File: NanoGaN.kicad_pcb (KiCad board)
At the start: 6 copper layers, 54 x 94 mm, 221 parts, among them J1 U_DC, J10 Conn_01x06, J11 Conn_01x04, J12 USB4085-GF-A, J14 Conn_01x03, J2 GND, J3 Phase_U, J4 Phase_V, J5 Phase_W, J6 FTSH-107-01-L-DV-K-TR, J7 Conn_01x03, J8 Conn_01x02, J9 Conn_01x07, Q1 IGC025S08S1, Q2 IGC025S08S1, Q3 IGC025S08S1, Q4 IGC025S08S1, Q5 IGC025S08S1, Q6 IGC025S08S1, Q7 Si2302CDS, U1 STM32H723VGTx, U10 SN74LVC1G66DCKR, U11 SN74LVC1G66DCKR, U12 LMG1205YFXR, U13 BMI323, U14 AS5047P-ATST, U15 TCAN1044VDRQ1, U16 SN74LVC1G66DCKR, U17 AD8418, U18 SN74LVC1G66DCKR, U19 NCS2220AMUT1G, U2 LMR51635XDDCR, U20 NCS2220AMUT1G, U21 NCS2220AMUT1G, U3 AMS1117, U4 AD8418, U5 LMG1205YFXR, U6 SN74LVC1G66DCKR, U7 SN74LVC1G66DCKR, U8 LMG1205YFXR, U9 AD8418, X1 8MHz

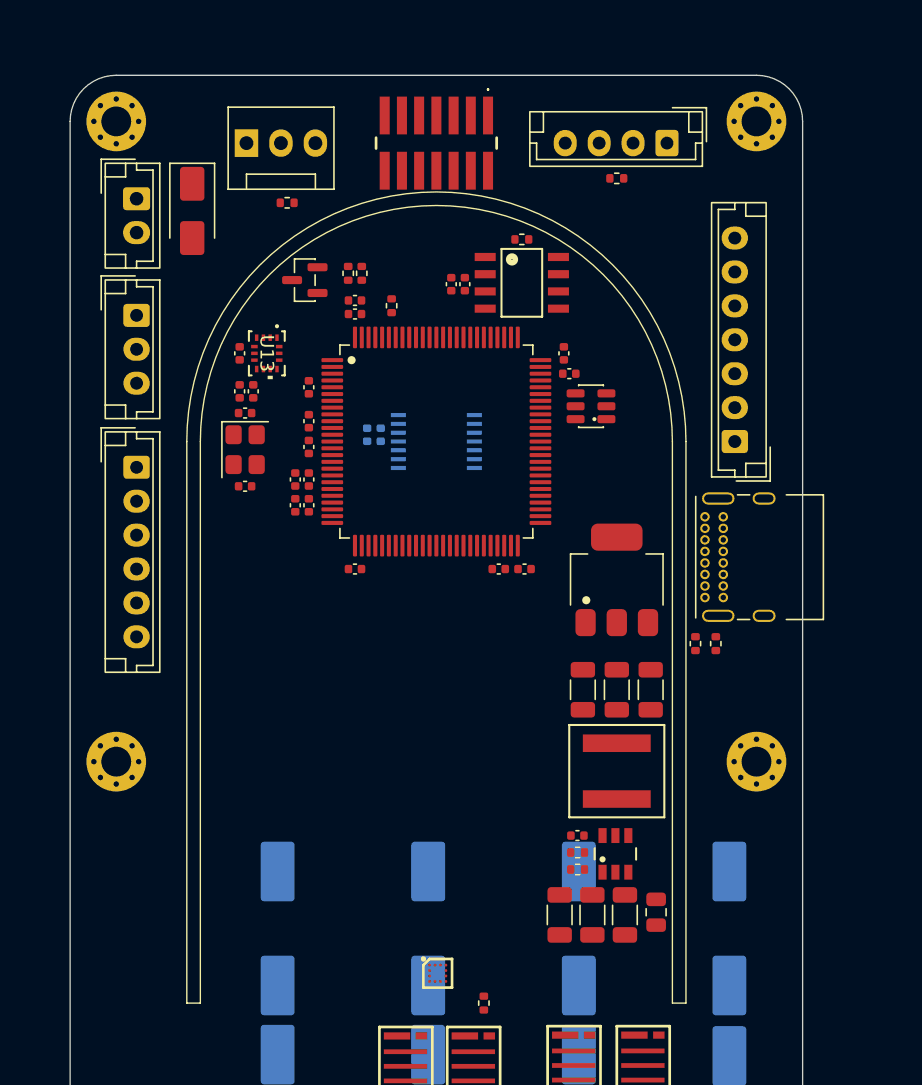
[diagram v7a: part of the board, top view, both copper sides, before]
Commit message: added step file of cooling channel and modified the layout
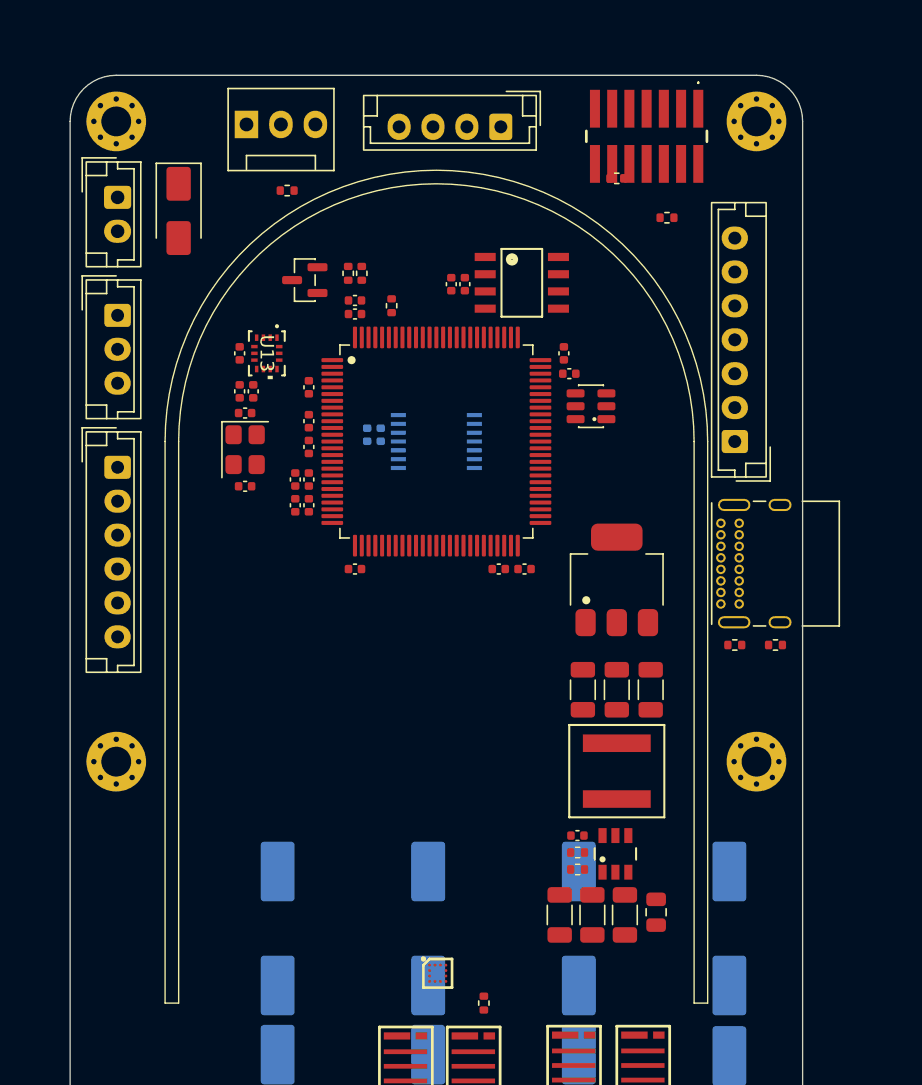
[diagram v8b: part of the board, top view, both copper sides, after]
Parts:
- moved J6 15.5 mm to (160.7, 52.5)
- moved J11 12.3 mm to (149.9, 51.8)
- moved R7 10.8 mm to (162.2, 58.5)
- moved R37 4.40 mm to (170.2, 90.0), turned to 0 degrees
- moved R38 2.90 mm to (167.2, 90.0), turned to 0 degrees
- moved J8 1.40 mm to (121.7, 57.0)
- moved J10 1.40 mm to (121.7, 76.9)
- moved J7 1.40 mm to (121.7, 65.7)
- moved J14 1.38 mm to (131.2, 51.6)
- moved J12 1.27 mm to (166.1, 87.0)
- moved D3 1.00 mm to (126.2, 58.0)
- moved R50 0.90 mm to (134.2, 56.5)
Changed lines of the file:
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@@
 	(footprint "Connector_JST:JST_EH_B3B-EH-A_1x03_P2.50mm_Vertical"
 		(layer "F.Cu")
-		(at 123.0651 65.7 -90)
+		(at 121.6651 65.7 -90)
 		(descr "JST EH series connector, B3B-EH-A (http://www.jst-mfg.com/product/pdf/eng/eEH.pdf), generated with kicad-footprint-generator")
 		(tags "connector JST EH vertical")
@@
 	(footprint "Connector:FanPinHeader_1x03_P2.54mm_Vertical"
 		(layer "F.Cu")
-		(at 131.1651 53)
+		(at 131.1651 51.625)
 		(descr "3-pin CPU fan Through hole pin header, see http://www.formfactors.org/developer%5Cspecs%5Crev1_2_public.pdf")
 		(tags "pin header 3-pin CPU fan")
@@
 	(footprint "Connector_USB:USB_C_Receptacle_GCT_USB4085"
 		(layer "F.Cu")
-		(at 164.9651 86.5 90)
+		(at 166.1401 86.975 90)
 		(descr "USB 2.0 Type C Receptacle, https://gct.co/Files/Drawings/USB4085.pdf")
 		(tags "USB Type-C Receptacle Through-hole Right angle")
@@
 	(footprint "Connector_JST:JST_EH_B2B-EH-A_1x02_P2.50mm_Vertical"
 		(layer "F.Cu")
-		(at 123.0651 57.1 -90)
+		(at 121.6651 57 -90)
 		(descr "JST EH series connector, B2B-EH-A (http://www.jst-mfg.com/product/pdf/eng/eEH.pdf), generated with kicad-footprint-generator")
 		(tags "connector JST EH vertical")
@@
 	(footprint "NanoGaN:FTSH10701LDVKTR"
 		(layer "F.Cu")
-		(at 145.1651 53 180)
+		(at 160.6651 52.5 180)
 		(descr "FTSH-107-01-L-DV-K-TR-3")
 		(tags "Connector")
@@
 	(footprint "Connector_JST:JST_EH_B4B-EH-A_1x04_P2.50mm_Vertical"
 		(layer "F.Cu")
-		(at 162.1651 53 180)
+		(at 149.9151 51.8 180)
 		(descr "JST EH series connector, B4B-EH-A (http://www.jst-mfg.com/product/pdf/eng/eEH.pdf), generated with kicad-footprint-generator")
 		(tags "connector JST EH vertical")
@@
 	(footprint "Connector_JST:JST_EH_B6B-EH-A_1x06_P2.50mm_Vertical"
 		(layer "F.Cu")
-		(at 123.0651 76.9 -90)
+		(at 121.6651 76.9 -90)
 		(descr "JST EH series connector, B6B-EH-A (http://www.jst-mfg.com/product/pdf/eng/eEH.pdf), generated with kicad-footprint-generator")
 		(tags "connector JST EH vertical")
@@
 	(footprint "Resistor_SMD:R_0402_1005Metric"
 		(layer "F.Cu")
-		(at 134.1651 57.4)
+		(at 134.1651 56.5)
 		(descr "Resistor SMD 0402 (1005 Metric), square (rectangular) end terminal, IPC-7351 nominal, (Body size source: IPC-SM-782 page 72, https://www.pcb-3d.com/wordpress/wp-content/uploads/ipc-sm-782a_amendment_1_and_2.pdf), generated with kicad-footprint-generator")
 		(tags "resistor")
@@
 	(footprint "Resistor_SMD:R_0402_1005Metric"
 		(layer "F.Cu")
-		(at 164.2651 89.9 -90)
+		(at 167.1651 90)
 		(descr "Resistor SMD 0402 (1005 Metric), square (rectangular) end terminal, IPC-7351 nominal, (Body size source: IPC-SM-782 page 72, https://www.pcb-3d.com/wordpress/wp-content/uploads/ipc-sm-782a_amendment_1_and_2.pdf), generated with kicad-footprint-generator")
 		(tags "resistor")
 		(property "Reference" "R38"
-			(at 0 -1.17 90)
+			(at 0 -1.17 0)
 			(layer "F.SilkS")
 			(hide yes)
@@
 		)
 		(property "Value" "5k1"
-			(at 0 1.17 90)
+			(at 0 1.17 0)
 			(layer "F.Fab")
 			(hide yes)
@@
 		)
 		(property "Datasheet" "~"
-			(at 0 0 90)
+			(at 0 0 0)
 			(layer "F.Fab")
 			(hide yes)
@@
 		)
 		(property "Description" "-55℃~+155℃ 5.1kΩ 50V 62.5mW Thick Film Resistor ±1% ±100ppm/℃ 0402 Chip Resistor - Surface Mount ROHS"
-			(at 0 0 90)
+			(at 0 0 0)
 			(layer "F.Fab")
 			(hide yes)
@@
 		)
 		(property "LCSC" "C25905"
-			(at 0 0 270)
+			(at 0 0 0)
 			(unlocked yes)
 			(layer "F.Fab")
@@
 		(attr smd)
 		(fp_line
-			(start -0.153641 0.38)
-			(end 0.153641 0.38)
+			(start -0.153641 -0.38)
+			(end 0.153641 -0.38)
 			(stroke
 				(width 0.12)
@@
 		)
 		(fp_line
-			(start -0.153641 -0.38)
-			(end 0.153641 -0.38)
+			(start -0.153641 0.38)
+			(end 0.153641 0.38)
 			(stroke
 				(width 0.12)
@@
 		)
 		(fp_text user "${REFERENCE}"
-			(at 0 0 90)
+			(at 0 0 0)
 			(layer "F.Fab")
 			(effects
@@
 		)
 		(pad "1" smd roundrect
-			(at -0.51 0 270)
+			(at -0.51 0)
 			(size 0.54 0.64)
 			(layers "F.Cu" "F.Mask" "F.Paste")
@@
 		)
 		(pad "2" smd roundrect
-			(at 0.51 0 270)
+			(at 0.51 0)
 			(size 0.54 0.64)
 			(layers "F.Cu" "F.Mask" "F.Paste")
@@
 	(footprint "Diode_SMD:D_SMA"
 		(layer "F.Cu")
-		(at 127.1651 58 -90)
+		(at 126.1651 58 -90)
 		(descr "Diode SMA (DO-214AC)")
 		(tags "Diode SMA (DO-214AC)")
@@
 	(footprint "Resistor_SMD:R_0402_1005Metric"
 		(layer "F.Cu")
-		(at 151.4651 60.1 180)
+		(at 162.1651 58.5 180)
 		(descr "Resistor SMD 0402 (1005 Metric), square (rectangular) end terminal, IPC-7351 nominal, (Body size source: IPC-SM-782 page 72, https://www.pcb-3d.com/wordpress/wp-content/uploads/ipc-sm-782a_amendment_1_and_2.pdf), generated with kicad-footprint-generator")
 		(tags "resistor")
@@
 	(footprint "Resistor_SMD:R_0402_1005Metric"
 		(layer "F.Cu")
-		(at 165.7651 89.9 -90)
+		(at 170.1651 90)
 		(descr "Resistor SMD 0402 (1005 Metric), square (rectangular) end terminal, IPC-7351 nominal, (Body size source: IPC-SM-782 page 72, https://www.pcb-3d.com/wordpress/wp-content/uploads/ipc-sm-782a_amendment_1_and_2.pdf), generated with kicad-footprint-generator")
 		(tags "resistor")
 		(property "Reference" "R37"
-			(at 0 -1.17 90)
+			(at 0 -1.17 0)
 			(layer "F.SilkS")
 			(hide yes)
@@
 		)
 		(property "Value" "5k1"
-			(at 0 1.17 90)
+			(at 0 1.17 0)
 			(layer "F.Fab")
 			(hide yes)
@@
 		)
 		(property "Datasheet" "~"
-			(at 0 0 90)
+			(at 0 0 0)
 			(layer "F.Fab")
 			(hide yes)
@@
 		)
 		(property "Description" "-55℃~+155℃ 5.1kΩ 50V 62.5mW Thick Film Resistor ±1% ±100ppm/℃ 0402 Chip Resistor - Surface Mount ROHS"
-			(at 0 0 90)
+			(at 0 0 0)
 			(layer "F.Fab")
 			(hide yes)
@@
 		)
 		(property "LCSC" "C25905"
-			(at 0 0 270)
+			(at 0 0 0)
 			(unlocked yes)
 			(layer "F.Fab")
@@
 		(attr smd)
 		(fp_line
-			(start -0.153641 0.38)
-			(end 0.153641 0.38)
+			(start -0.153641 -0.38)
+			(end 0.153641 -0.38)
 			(stroke
 				(width 0.12)
@@
 		)
 		(fp_line
-			(start -0.153641 -0.38)
-			(end 0.153641 -0.38)
+			(start -0.153641 0.38)
+			(end 0.153641 0.38)
 			(stroke
 				(width 0.12)
@@
 		)
 		(fp_text user "${REFERENCE}"
-			(at 0 0 90)
+			(at 0 0 0)
 			(layer "F.Fab")
 			(effects
@@
 		)
 		(pad "1" smd roundrect
-			(at -0.51 0 270)
+			(at -0.51 0)
 			(size 0.54 0.64)
 			(layers "F.Cu" "F.Mask" "F.Paste")
@@
 		)
 		(pad "2" smd roundrect
-			(at 0.51 0 270)
+			(at 0.51 0)
 			(size 0.54 0.64)
 			(layers "F.Cu" "F.Mask" "F.Paste")
@@
 	)
 	(gr_line
-		(start 163.5651 75)
-		(end 163.5651 116.4)
+		(start 165.1651 75)
+		(end 165.1651 116.4)
 		(stroke
 			(width 0.1)
@@
 	)
 	(gr_line
-		(start 162.5651 116.4)
-		(end 163.5651 116.4)
+		(start 164.1651 116.4)
+		(end 165.1651 116.4)
 		(stroke
 			(width 0.1)
@@
 	)
 	(gr_arc
-		(start 127.7651 75)
-		(mid 145.1651 57.6)
-		(end 162.5651 75)
+		(start 126.1651 75)
+		(mid 145.1651 56)
+		(end 164.1651 75)
 		(stroke
 			(width 0.1)
@@
 	)
 	(gr_arc
-		(start 126.7651 75)
-		(mid 145.1651 56.6)
-		(end 163.5651 75)
+		(start 125.1651 75)
+		(mid 145.1651 55)
+		(end 165.1651 75)
 		(stroke
 			(width 0.1)
@@
 	)
 	(gr_line
-		(start 127.7651 75)
-		(end 127.7651 116.4)
+		(start 126.1651 75)
+		(end 126.1651 116.4)
 		(stroke
 			(width 0.1)
@@
 	)
 	(gr_line
-		(start 127.7651 116.4)
-		(end 126.7651 116.4)
+		(start 126.1651 116.4)
+		(end 125.1651 116.4)
 		(stroke
 			(width 0.1)
@@
 	)
 	(gr_line
-		(start 162.5651 75)
-		(end 162.5651 116.4)
+		(start 164.1651 75)
+		(end 164.1651 116.4)
 		(stroke
 			(width 0.1)
@@
 	)
 	(gr_line
-		(start 126.7651 75)
-		(end 126.7651 116.4)
+		(start 125.1651 75)
+		(end 125.1651 116.4)
 		(stroke
 			(width 0.1)
